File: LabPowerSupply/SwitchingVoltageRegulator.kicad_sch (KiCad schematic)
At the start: 14 parts

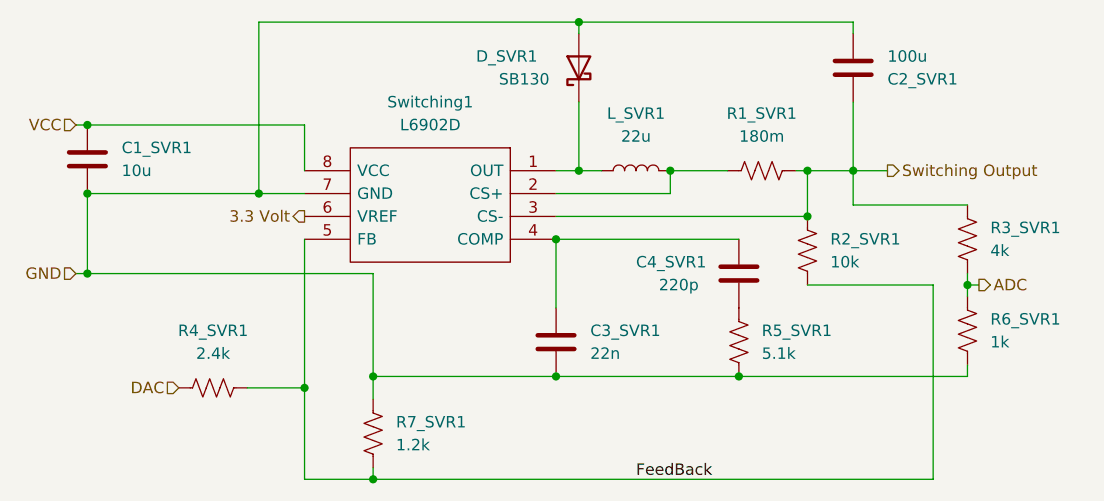
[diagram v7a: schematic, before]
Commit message: Changed most parts to smd
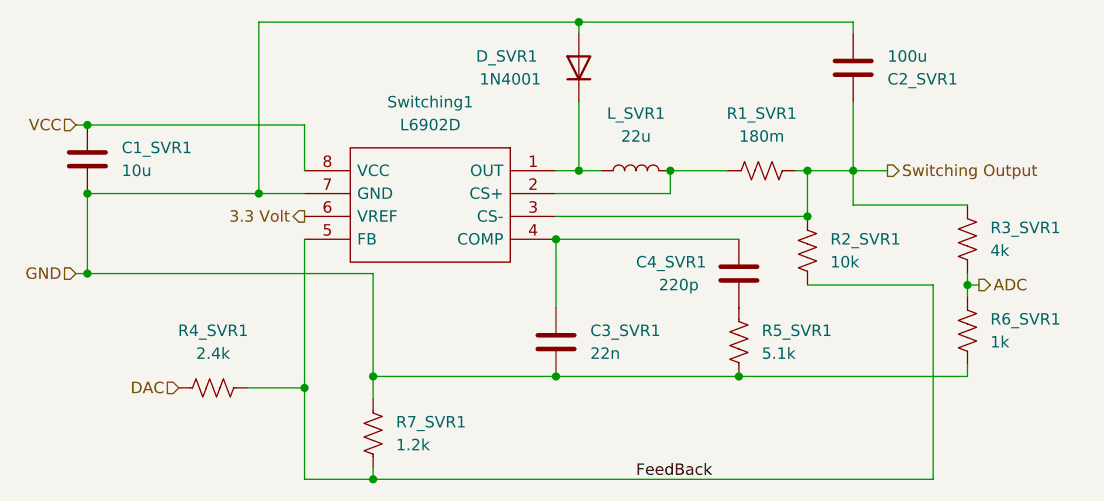
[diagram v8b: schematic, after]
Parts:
- C1_SVR1: footprint Capacitor_THT:C_Disc_D5.0mm_W2.5mm_P2.50mm -> Capacitor_SMD:C_0805_2012Metric
- C3_SVR1, C4_SVR1: footprint Capacitor_THT:C_Disc_D7.5mm_W2.5mm_P5.00mm -> Capacitor_SMD:C_0805_2012Metric
- D_SVR1: value SB130 -> 1N4001; footprint Diode_THT:D_DO-41_SOD81_P10.16mm_Horizontal -> Diode_SMD:D_SMA; symbol Diode:SB130 -> Diode:1N4001
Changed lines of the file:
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@@
     (pin "2")
   )
-  (symbol (lib_id "Diode:SB130") (at 140.97 81.28 90) (unit 1)
+  (symbol (lib_id "Diode:1N4001") (at 140.97 81.28 90) (unit 1)
     (in_bom yes) (on_board yes)
     (property "Reference" "D_SVR1" (id 0) (at 129.54 80.01 90)
       (effects (font (size 1.27 1.27)) (justify right))
     )
-    (property "Value" "SB130" (id 1) (at 132.08 82.55 90)
-      (effects (font (size 1.27 1.27)) (justify right))
-    )
-    (property "Footprint" "Diode_THT:D_DO-41_SOD81_P10.16mm_Horizontal" (id 2) (at 145.415 81.28 0)
+    (property "Value" "1N4001" (id 1) (at 133.35 82.55 90))
+    (property "Footprint" "Diode_SMD:D_SMA" (id 2) (at 145.415 81.28 0)
       (effects (font (size 1.27 1.27)) hide)
     )
-    (property "Datasheet" "http://www.diodes.com/_files/datasheets/ds23022.pdf" (id 3) (at 140.97 81.28 0)
+    (property "Datasheet" "http://www.vishay.com/docs/88503/1n4001.pdf" (id 3) (at 140.97 81.28 0)
       (effects (font (size 1.27 1.27)) hide)
     )
@@
       (effects (font (size 1.27 1.27)) (justify left))
     )
-    (property "Footprint" "Capacitor_THT:C_Disc_D7.5mm_W2.5mm_P5.00mm" (id 2) (at 139.3952 115.57 0)
+    (property "Footprint" "Capacitor_SMD:C_0805_2012Metric" (id 2) (at 139.3952 115.57 0)
       (effects (font (size 1.27 1.27)) hide)
     )
@@
       (effects (font (size 1.27 1.27)) (justify left))
     )
-    (property "Footprint" "Capacitor_THT:C_Disc_D5.0mm_W2.5mm_P2.50mm" (id 2) (at 87.3252 95.25 0)
+    (property "Footprint" "Capacitor_SMD:C_0805_2012Metric" (id 2) (at 87.3252 95.25 0)
       (effects (font (size 1.27 1.27)) hide)
     )
@@
       (effects (font (size 1.27 1.27)) (justify left))
     )
-    (property "Footprint" "Capacitor_THT:C_Disc_D7.5mm_W2.5mm_P5.00mm" (id 2) (at 159.7152 107.95 0)
+    (property "Footprint" "Capacitor_SMD:C_0805_2012Metric" (id 2) (at 159.7152 107.95 0)
       (effects (font (size 1.27 1.27)) hide)
     )
